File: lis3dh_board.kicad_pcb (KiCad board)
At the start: 2 copper layers, 102.9 x 25.4 mm, 25 parts, among them J1 T4_IF, J2 BQ25798_BOARD, J3 WL-125, J4 RFID_ANT, Q1 BSS138, U1 TLV75530PDBV, U2 LIS3DH

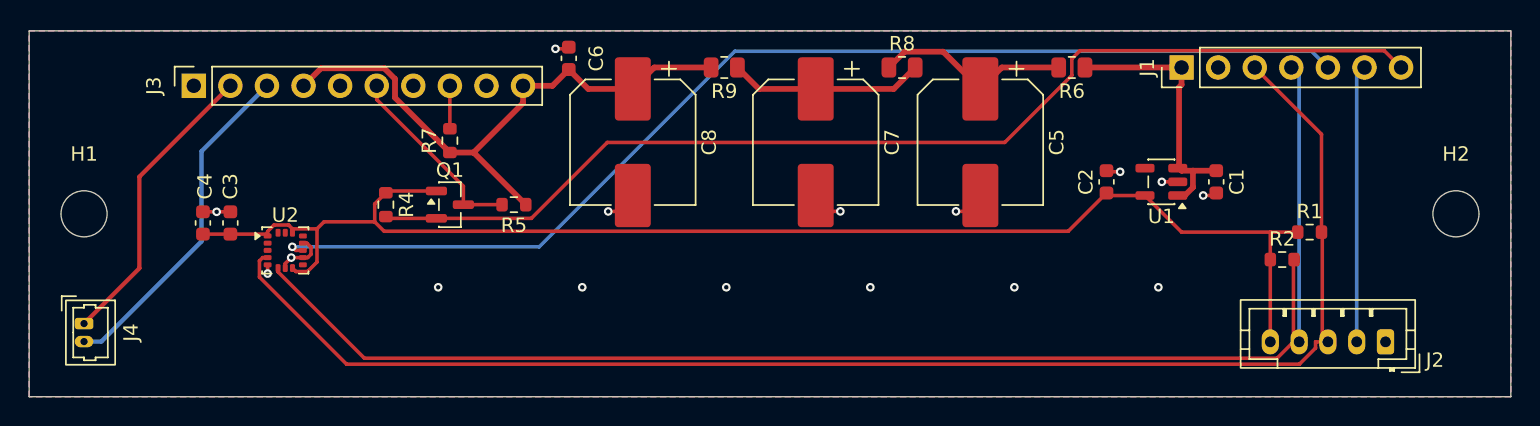
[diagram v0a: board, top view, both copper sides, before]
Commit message: Route the PCB
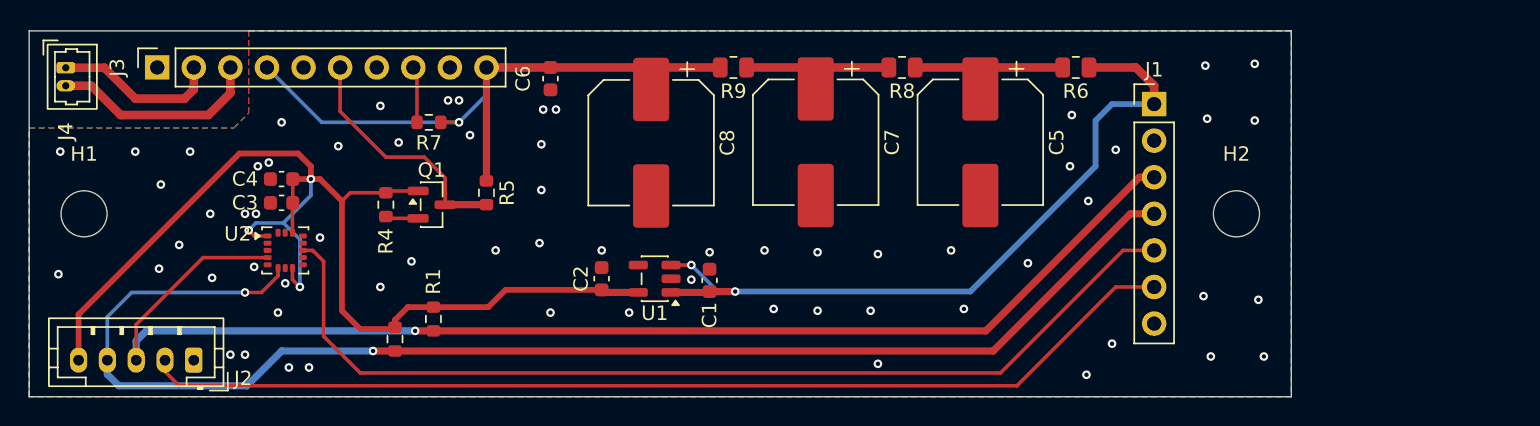
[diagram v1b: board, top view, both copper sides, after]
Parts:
- moved J2 82.7 mm to (113.0, 99.1)
- moved R2 61.8 mm to (127.0, 97.6), turned to -90 degrees
- moved R1 61.1 mm to (129.7, 96.2), turned to -90 degrees
- moved C1 35.8 mm to (148.8, 93.5), turned to 90 degrees
- moved U1 35.8 mm to (145.0, 93.4)
- moved C2 35.7 mm to (141.3, 93.4)
- moved J4 17.8 mm to (104.1, 78.8)
- moved H2 15.2 mm to (185.4, 88.9)
- moved C4 6.25 mm to (119.1, 86.5), turned to 180 degrees
- moved C3 3.82 mm to (119.1, 88.1), turned to 180 degrees
- moved J1 3.18 mm to (179.7, 81.3), turned to 0 degrees
- moved J3 2.84 mm to (110.5, 78.7)
- moved R5 2.08 mm to (133.3, 87.4), turned to -90 degrees
- moved R7 1.94 mm to (129.3, 82.5), turned to 180 degrees
- moved C6 1.90 mm to (137.8, 79.5), turned to -90 degrees
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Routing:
- net /RFID_TX: track 76.5 -> 2.29 mm
- net /CHG_INT: track 19.3 -> 72.7 mm
- net +5V: track 19.0 -> 52.3 mm, vias 0 -> 2
- net GND: track 16.6 -> 0.00 mm, vias 16 -> 65
- net +3V0: track 97.5 -> 83.2 mm, vias 0 -> 3
- net /SCL: track 100.4 -> 90.2 mm, vias 0 -> 1
- net /INT1: track 78.8 -> 69.2 mm, vias 1 -> 0
- net /ANT1: track 20.7 -> 11.6 mm
- net /ANT2: track 23.7 -> 14.7 mm
- net /VCC_RF: track 41.4 -> 48.6 mm, vias 0 -> 1
- net /SDA: track 99.1 -> 95.5 mm, vias 0 -> 2
- net /RFID_TX_5V: track 13.4 -> 17.0 mm
- net /VRF2: track 13.6 -> 12.0 mm
- net /VRF1: track 13.9 -> 12.4 mm
- net /RFID_RST: track 2.98 -> 3.92 mm
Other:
- board size 102.9 x 25.4 mm -> 87.6 x 25.4 mm
